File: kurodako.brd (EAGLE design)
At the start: 92 x 71 mm, 42 parts, among them J1 CONN-4P-MICROMATCH-SMD, J10 CONN-4P-MICROMATCH-SMD, J11 CONN-4P-MICROMATCH-SMD, J12 CONN-4P-MICROMATCH-SMD, J13 CONN-4P-MICROMATCH-SMD, J14 CONN-4P-MICROMATCH-SMD, J15 CONN-4P-MICROMATCH-SMD, J16 CONN-4P-MICROMATCH-SMD, J2 CONN-4P-MICROMATCH-SMD, J3 CONN-4P-MICROMATCH-SMD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

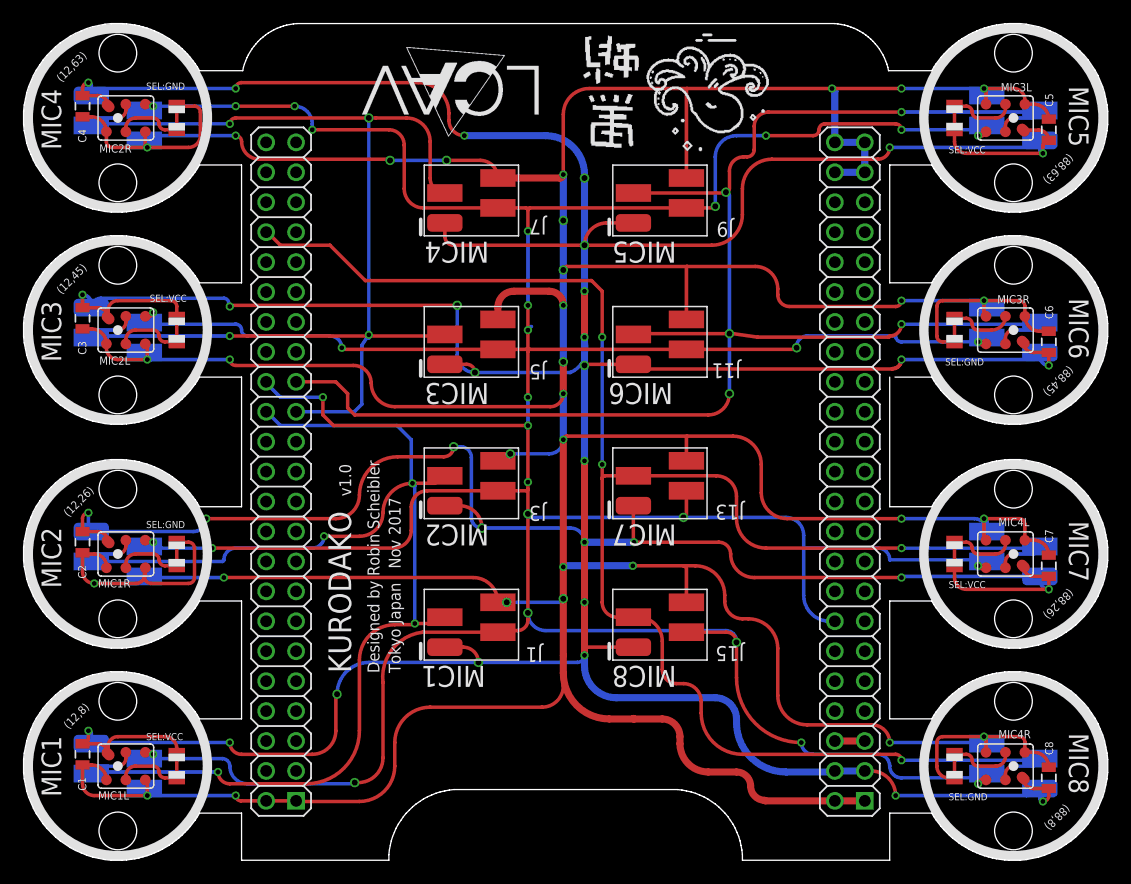
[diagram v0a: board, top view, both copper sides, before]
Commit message: Added resistors on mic high and possiblity to change pdm clk.
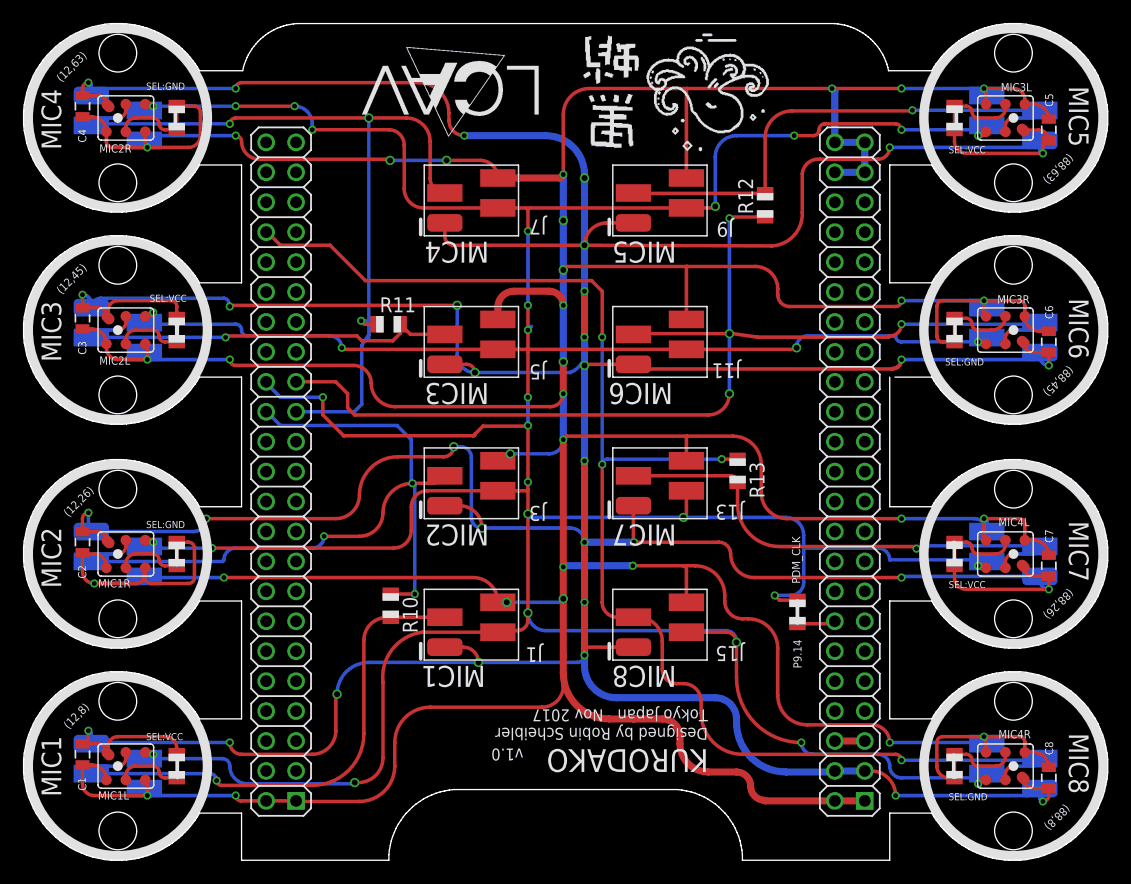
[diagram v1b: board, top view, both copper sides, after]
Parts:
- added R10, R11, R12, R13: 100, adafruit:R0805
- added R9: (no value), adafruit:R0805
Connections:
- new net DAT1_H: J1.3, J2.3, MIC1L.DAT, R10.2
- new net DAT2_H: J5.3, J6.3, MIC2L.DAT, R11.2
- new net DAT3_H: J10.3, J9.3, MIC3L.DAT, R12.2
- new net DAT4_H: J13.3, J14.3, MIC4L.DAT, R13.2
- net DAT1: now also R10.1; no longer J1.3, J2.3, MIC1L.DAT
- net DAT2: now also R11.1; no longer J5.3, J6.3, MIC2L.DAT
- net DAT3: now also R12.1; no longer J10.3, J9.3, MIC3L.DAT
- net DAT4: now also R13.1; no longer J13.3, J14.3, MIC4L.DAT
- net PDM_CLK: now also R9.1, R9.2
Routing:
- net DAT1_H: track 0.00 -> 44.9 mm, vias 0 -> 2
- net DAT1: track 110.1 -> 65.9 mm, vias 6 -> 4
- net DAT3_H: track 0.00 -> 44.2 mm, vias 0 -> 2
- net DAT3: track 139.1 -> 96.4 mm, vias 7 -> 5
- net DAT4_H: track 0.00 -> 42.4 mm, vias 0 -> 2
- net DAT2_H: track 0.00 -> 35.6 mm, vias 0 -> 2
- net DAT4: track 150.6 -> 117.4 mm, vias 6 -> 5
- net DAT2: track 103.5 -> 71.4 mm, vias 6 -> 4
- net PDM_CLK: track 412.5 -> 419.5 mm, vias 30 -> 31
- net VCC: track 548.1 -> 548.8 mm
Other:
- board text added: "P9.14"
- board text added: "PDM_CLK"

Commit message: Added some values for the components on the schematics, a pdf of the schematics and the BOM.
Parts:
- C1, C2, C3, C4, C5, C6, C7, C8: value (none) -> 0.1uF
- R1, R2, R3, R4, R5, R6, R7, R8, R9: value (none) -> DNI
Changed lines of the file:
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@@
 </autorouter>
 <elements>
-<element name="C1" library="SparkFun" package="0805" value="" x="9" y="9" smashed="yes" rot="R270">
+<element name="C1" library="SparkFun" package="0805" value="0.1uF" x="9" y="9" smashed="yes" rot="R270">
 <attribute name="NAME" x="8.6255" y="7.062" size="0.7" layer="25" rot="R270"/>
 <attribute name="VALUE" x="7.603" y="10.016" size="0.4064" layer="27" rot="R270"/>
 </element>
-<element name="C2" library="SparkFun" package="0805" value="" x="9" y="27" smashed="yes" rot="R270">
+<element name="C2" library="SparkFun" package="0805" value="0.1uF" x="9" y="27" smashed="yes" rot="R270">
 <attribute name="NAME" x="8.6255" y="25.062" size="0.7" layer="25" rot="R270"/>
 <attribute name="VALUE" x="7.603" y="28.016" size="0.4064" layer="27" rot="R270"/>
 </element>
-<element name="C3" library="SparkFun" package="0805" value="" x="9" y="46" smashed="yes" rot="R270">
+<element name="C3" library="SparkFun" package="0805" value="0.1uF" x="9" y="46" smashed="yes" rot="R270">
 <attribute name="NAME" x="8.6255" y="44.062" size="0.7" layer="25" rot="R270"/>
 <attribute name="VALUE" x="7.603" y="47.016" size="0.4064" layer="27" rot="R270"/>
 </element>
-<element name="C4" library="SparkFun" package="0805" value="" x="9" y="64" smashed="yes" rot="R270">
+<element name="C4" library="SparkFun" package="0805" value="0.1uF" x="9" y="64" smashed="yes" rot="R270">
 <attribute name="NAME" x="8.6255" y="62.062" size="0.7" layer="25" rot="R270"/>
 <attribute name="VALUE" x="7.603" y="65.016" size="0.4064" layer="27" rot="R270"/>
 </element>
-<element name="C5" library="SparkFun" package="0805" value="" x="91" y="62" smashed="yes" rot="R90">
+<element name="C5" library="SparkFun" package="0805" value="0.1uF" x="91" y="62" smashed="yes" rot="R90">
 <attribute name="NAME" x="91.3745" y="63.938" size="0.7" layer="25" rot="R90"/>
 <attribute name="VALUE" x="92.397" y="60.984" size="0.4064" layer="27" rot="R90"/>
 </element>
-<element name="C6" library="SparkFun" package="0805" value="" x="91" y="44" smashed="yes" rot="R90">
+<element name="C6" library="SparkFun" package="0805" value="0.1uF" x="91" y="44" smashed="yes" rot="R90">
 <attribute name="NAME" x="91.3745" y="45.938" size="0.7" layer="25" rot="R90"/>
 <attribute name="VALUE" x="92.397" y="42.984" size="0.4064" layer="27" rot="R90"/>
 </element>
-<element name="C7" library="SparkFun" package="0805" value="" x="91" y="25" smashed="yes" rot="R90">
+<element name="C7" library="SparkFun" package="0805" value="0.1uF" x="91" y="25" smashed="yes" rot="R90">
 <attribute name="NAME" x="91.3745" y="26.938" size="0.7" layer="25" rot="R90"/>
 <attribute name="VALUE" x="92.397" y="23.984" size="0.4064" layer="27" rot="R90"/>
 </element>
-<element name="C8" library="SparkFun" package="0805" value="" x="91" y="7" smashed="yes" rot="R90">
+<element name="C8" library="SparkFun" package="0805" value="0.1uF" x="91" y="7" smashed="yes" rot="R90">
 <attribute name="NAME" x="91.3745" y="8.938" size="0.7" layer="25" rot="R90"/>
 <attribute name="VALUE" x="92.397" y="5.984" size="0.4064" layer="27" rot="R90"/>
@@
 <attribute name="NAME" x="86.72" y="10.36" size="0.7" layer="25"/>
 </element>
-<element name="R1" library="adafruit" package="R0805" value="" x="17" y="8" smashed="yes" rot="R90">
+<element name="R1" library="adafruit" package="R0805" value="DNI" x="17" y="8" smashed="yes" rot="R90">
 <attribute name="VALUE" x="19.286" y="7.238" size="1.27" layer="27" rot="R90"/>
 </element>
-<element name="R2" library="adafruit" package="R0805" value="" x="17" y="26" smashed="yes" rot="R90">
+<element name="R2" library="adafruit" package="R0805" value="DNI" x="17" y="26" smashed="yes" rot="R90">
 <attribute name="VALUE" x="19.286" y="25.238" size="1.27" layer="27" rot="R90"/>
 </element>
-<element name="R3" library="adafruit" package="R0805" value="" x="17" y="45" smashed="yes" rot="R90">
+<element name="R3" library="adafruit" package="R0805" value="DNI" x="17" y="45" smashed="yes" rot="R90">
 <attribute name="VALUE" x="19.286" y="44.238" size="1.27" layer="27" rot="R90"/>
 </element>
-<element name="R4" library="adafruit" package="R0805" value="" x="17" y="63" smashed="yes" rot="R90">
+<element name="R4" library="adafruit" package="R0805" value="DNI" x="17" y="63" smashed="yes" rot="R90">
 <attribute name="VALUE" x="19.286" y="62.238" size="1.27" layer="27" rot="R90"/>
 </element>
-<element name="R5" library="adafruit" package="R0805" value="" x="83" y="63" smashed="yes" rot="R270">
+<element name="R5" library="adafruit" package="R0805" value="DNI" x="83" y="63" smashed="yes" rot="R270">
 <attribute name="VALUE" x="80.714" y="63.762" size="1.27" layer="27" rot="R270"/>
 </element>
-<element name="R6" library="adafruit" package="R0805" value="" x="83" y="45" smashed="yes" rot="R270">
+<element name="R6" library="adafruit" package="R0805" value="DNI" x="83" y="45" smashed="yes" rot="R270">
 <attribute name="VALUE" x="80.714" y="45.762" size="1.27" layer="27" rot="R270"/>
 </element>
-<element name="R7" library="adafruit" package="R0805" value="" x="83" y="26" smashed="yes" rot="R270">
+<element name="R7" library="adafruit" package="R0805" value="DNI" x="83" y="26" smashed="yes" rot="R270">
 <attribute name="VALUE" x="80.714" y="26.762" size="1.27" layer="27" rot="R270"/>
 </element>
-<element name="R8" library="adafruit" package="R0805" value="" x="83" y="8" smashed="yes" rot="R270">
+<element name="R8" library="adafruit" package="R0805" value="DNI" x="83" y="8" smashed="yes" rot="R270">
 <attribute name="VALUE" x="80.714" y="8.762" size="1.27" layer="27" rot="R270"/>
 </element>
 <element name="U$7" library="LCAV" package="BEAGLEBONE_SHIELD_NOCUT" value="BEAGLEBONE_OUTLINE-NOCUT" x="22.68" y="-14" smashed="yes"/>
 <element name="U$1" library="LCAV" package="LCAV_LOGO_15MM" value="" x="47.7" y="69" rot="R180"/>
-<element name="R9" library="adafruit" package="R0805" value="" x="69.6712" y="21.0824" smashed="yes" rot="R90">
+<element name="R9" library="adafruit" package="R0805" value="DNI" x="69.6712" y="21.0824" smashed="yes" rot="R90">
 <attribute name="VALUE" x="71.9572" y="20.3204" size="1.27" layer="27" rot="R90"/>
 </element>
